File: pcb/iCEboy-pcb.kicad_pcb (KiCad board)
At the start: 2 copper layers, 51 x 61 mm, 64 parts, among them J1 dmg-card, J2 PROG_PORT, Q1 2N7002K, U1 TC74LCXR163245FT, U2 TC74LCXR163245FT, U3 ICE40UP5K-SG48ITR, U4 TPS79901DDCR, U5 TPS79901DDCR, U6 W25Q80DVSSIG, X1 SIT2001B

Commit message: modify value fields
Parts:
- C17: value C -> DNP
- J1: value dmg-card -> DMG_CARD
- R10, R11, R12, R13, R2: value 10k -> 10kΩ
- R3: value 2.2k -> 2.2kΩ
- R7: value 100Ω -> 1kΩ
- R8, R9: value R -> DNP

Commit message: modify decoup C value
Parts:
- C22, C26: value 2.2μF -> 4.7μF

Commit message: change value of X1
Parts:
- X1: value SIT2001B -> SIT2001B 20MHz

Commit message: update LED current limiting resistors
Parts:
- D1: value YELLOW -> SML-E12Y8WT86
- D2: value RED -> SML-E12V8WT86
- D3: value GREEN -> SML-E12P8WT86
- D4: value BLUE -> SMLE13BC8TT86
- R5: value 2.2kΩ -> 680Ω
- R6: value 2.2kΩ -> 4.7kΩ

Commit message: swap C11 C14 value
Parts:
- C11: value 10nF -> 1μF
- C14: value 1μF -> 10nF

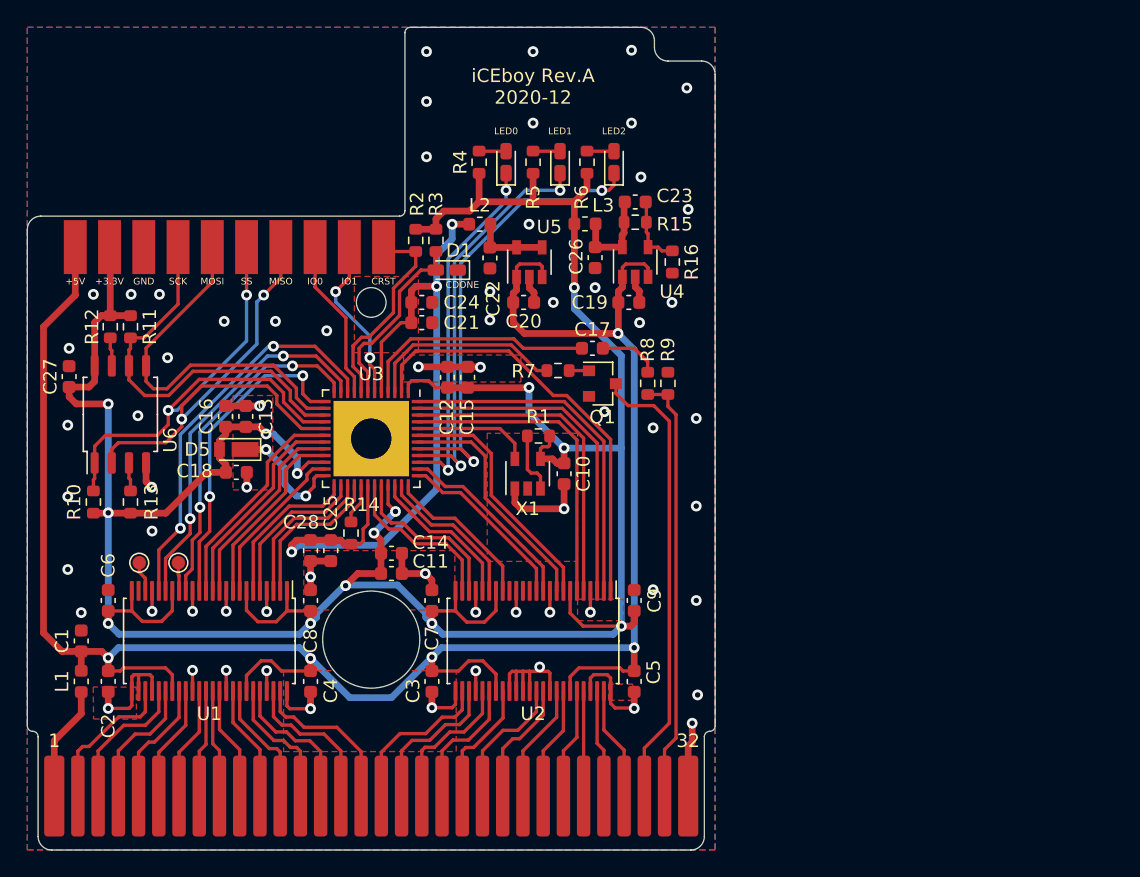
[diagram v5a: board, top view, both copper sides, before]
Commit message: migrate to KiCAD 6.0
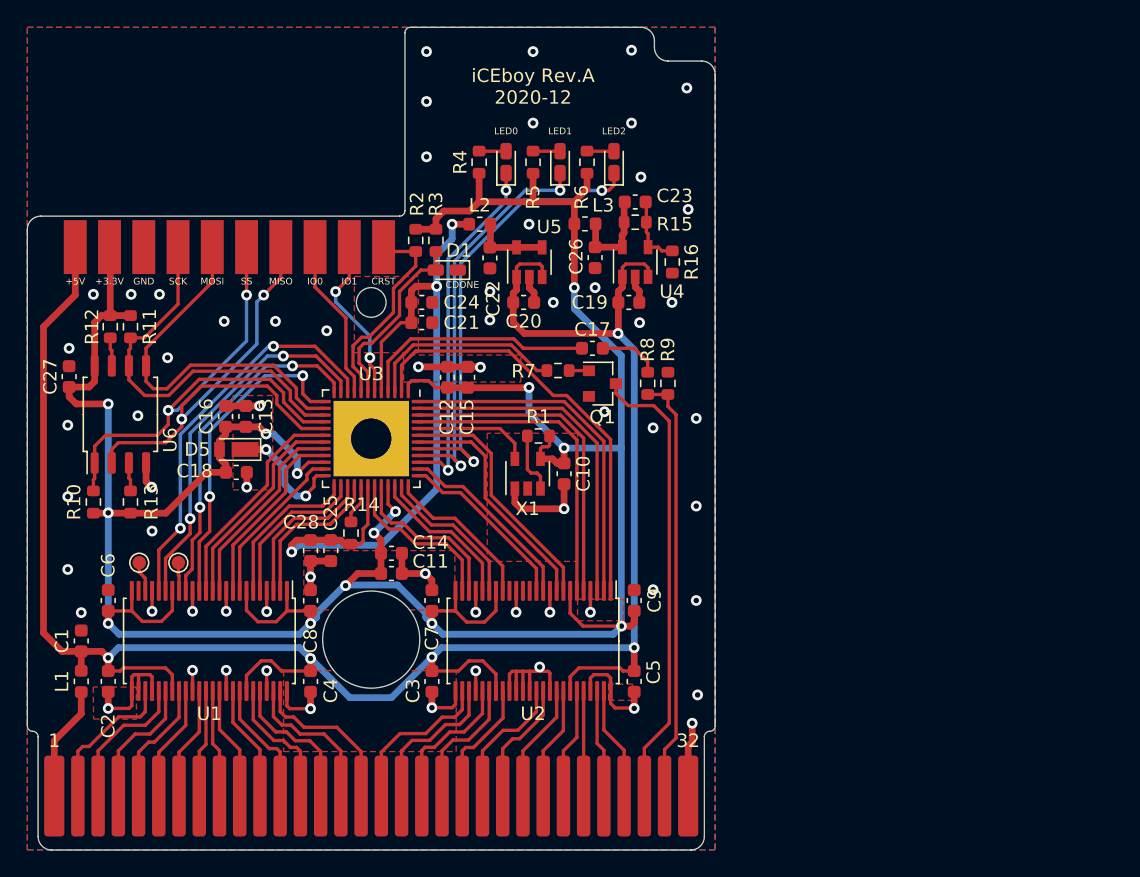
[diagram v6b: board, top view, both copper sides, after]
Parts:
- J1: value DMG_CARD -> DMG-CardEdge; footprint dmg-card:dmg-card -> DMG-CardEdge:DMG-CardEdge
- TP2: value ~CS -> ~{CS}
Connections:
- net /A0 renamed /CB-A0
- net /A0B renamed /DV-A0
- net /A1 renamed /CB-A1
- net /A10 renamed /CB-A10
- net /A10B renamed /DV-A10
- net /A11 renamed /CB-A11
- net /A11B renamed /DV-A11
- net /A12 renamed /CB-A12
- net /A12B renamed /DV-A12
- net /A13 renamed /CB-A13
- net /A13B renamed /DV-A13
- net /A14 renamed /CB-A14
- net /A14B renamed /DV-A14
- net /A15 renamed /CB-A15
- net /A15B renamed /DV-A15
- net /A1B renamed /DV-A1
- net /A2 renamed /CB-A2
- net /A2B renamed /DV-A2
- net /A3 renamed /CB-A3
- net /A3B renamed /DV-A3
- net /A4 renamed /CB-A4
- net /A4B renamed /DV-A4
- net /A5 renamed /CB-A5
- net /A5B renamed /DV-A5
- net /A6 renamed /CB-A6
- net /A6B renamed /DV-A6
- net /A7 renamed /CB-A7
- net /A7B renamed /DV-A7
- net /A8 renamed /CB-A8
- net /A8B renamed /DV-A8
- net /A9 renamed /CB-A9
- net /A9B renamed /DV-A9
- net /CLK renamed /CB-CLK
- net /CLKB renamed /DV-CLK
- net /D0 renamed /CB-D0
- net /D0B renamed /DV-D0
- net /D1 renamed /CB-D1
- net /D1B renamed /DV-D1
- net /D2 renamed /CB-D2
- net /D2B renamed /DV-D2
- net /D3 renamed /CB-D3
- net /D3B renamed /DV-D3
- net /D4 renamed /CB-D4
- net /D4B renamed /DV-D4
- net /D5 renamed /CB-D5
- net /D5B renamed /DV-D5
- net /D6 renamed /CB-D6
- net /D6B renamed /DV-D6
- net /D7 renamed /CB-D7
- net /D7B renamed /DV-D7
- net /EXT_CLK renamed /SYSCLK
- net /SPI_MISO renamed /SPI-MISO
- net /SPI_MOSI renamed /SPI-MOSI
- net /SPI_SCK renamed /SPI-SCK
- net /SPI_SS renamed /SPI-SS
- net /VIN renamed /CB-VIN
- net /VINB renamed /DV-VIN
- net /~CRESET renamed /~{CRESET}
- net /~CS renamed /CB-~{CS}
- net /~CS~B renamed /DV-~{CS}
- net /~RD renamed /CB-~{RD}
- net /~RD~B renamed /DV-~{RD}
- net /~RST renamed /CB-~{RST}
- net /~RST~B renamed /DV-~{RST}
- net /~WR renamed /CB-~{WR}
- net /~WR~B renamed /DV-~{WR}
- U1 pad 23: (no net) -> unconnected-(U1-Pad23)
- U2 pad 13: (no net) -> unconnected-(U2-Pad13)
- U2 pad 14: (no net) -> unconnected-(U2-Pad14)
- U2 pad 16: (no net) -> unconnected-(U2-Pad16)
- X1 pad 2: (no net) -> unconnected-(X1-Pad2)
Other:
- net class Bold removed
- net class Default removed

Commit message: update pcb wip
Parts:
- removed L1, L2, L3: 600Ω, Inductor_SMD:L_0603_1608Metric
- removed the R1 at (72.4, 64.8)
- removed the R9 at (82.0, 60.9)
- added C17: 1nF, Capacitor_SMD:C_0402_1005Metric, F.Cu at (113.2, 62.5)
- added C18: 1nF, Capacitor_SMD:C_0402_1005Metric, F.Cu at (113.2, 60.5)
- added FB1: MPZ1608S601ATA00, Inductor_SMD:L_0603_1608Metric, F.Cu at (38.9, 82.6)
- added FB2: MPZ1608S601ATA00, Inductor_SMD:L_0603_1608Metric, F.Cu at (68.0, 49.1)
- added FB3: MPZ1608S601ATA00, Inductor_SMD:L_0603_1608Metric, F.Cu at (75.8, 49.1)
- added R8: 8.2kΩ, Resistor_SMD:R_0402_1005Metric, F.Cu at (113.7, 58.0)
- C10, C12, C16, C2, C3, C4, C5, C6, C7, C8, C9: footprint Capacitor_SMD:C_0603_1608Metric -> Capacitor_SMD:C_0402_1005Metric
- C11: renamed from C15; footprint Capacitor_SMD:C_0603_1608Metric -> Capacitor_SMD:C_0402_1005Metric
- C13: renamed from C14; footprint Capacitor_SMD:C_0603_1608Metric -> Capacitor_SMD:C_0402_1005Metric
- C14: renamed from C13; footprint Capacitor_SMD:C_0603_1608Metric -> Capacitor_SMD:C_0402_1005Metric
- C15: renamed from C11; footprint Capacitor_SMD:C_0603_1608Metric -> Capacitor_SMD:C_0402_1005Metric
- C19: renamed from C17; value DNP -> 1uF; footprint Capacitor_SMD:C_0603_1608Metric -> Capacitor_SMD:C_0402_1005Metric
- C20: renamed from C18; footprint Capacitor_SMD:C_0603_1608Metric -> Capacitor_SMD:C_0402_1005Metric
- C21: renamed from C19; footprint Capacitor_SMD:C_0603_1608Metric -> Capacitor_SMD:C_0402_1005Metric
- C22: renamed from C20; footprint Capacitor_SMD:C_0603_1608Metric -> Capacitor_SMD:C_0402_1005Metric
- C23: renamed from C21; footprint Capacitor_SMD:C_0603_1608Metric -> Capacitor_SMD:C_0402_1005Metric
- C24: renamed from C22; footprint Capacitor_SMD:C_0603_1608Metric -> Capacitor_SMD:C_0402_1005Metric
- C25: renamed from C27; footprint Capacitor_SMD:C_0603_1608Metric -> Capacitor_SMD:C_0402_1005Metric
- C26: renamed from C24; footprint Capacitor_SMD:C_0603_1608Metric -> Capacitor_SMD:C_0402_1005Metric
- C27: renamed from C25; footprint Capacitor_SMD:C_0603_1608Metric -> Capacitor_SMD:C_0402_1005Metric
- C28: renamed from C23; footprint Capacitor_SMD:C_0603_1608Metric -> Capacitor_SMD:C_0402_1005Metric
- C30: renamed from C26; footprint Capacitor_SMD:C_0603_1608Metric -> Capacitor_SMD:C_0402_1005Metric
- R1: renamed from R2; footprint Resistor_SMD:R_0603_1608Metric -> Resistor_SMD:R_0402_1005Metric
- R10: renamed from R13; footprint Resistor_SMD:R_0603_1608Metric -> Resistor_SMD:R_0402_1005Metric
- R11, R12, R3: footprint Resistor_SMD:R_0603_1608Metric -> Resistor_SMD:R_0402_1005Metric
- R13: renamed from R14; footprint Resistor_SMD:R_0603_1608Metric -> Resistor_SMD:R_0402_1005Metric
- R14: renamed from R15; footprint Resistor_SMD:R_0603_1608Metric -> Resistor_SMD:R_0402_1005Metric
- R15: renamed from R16; footprint Resistor_SMD:R_0603_1608Metric -> Resistor_SMD:R_0402_1005Metric
- R2: renamed from R8; value DNP -> 8.2kΩ; footprint Resistor_SMD:R_0603_1608Metric -> Resistor_SMD:R_0402_1005Metric
- R4: renamed from R7; footprint Resistor_SMD:R_0603_1608Metric -> Resistor_SMD:R_0402_1005Metric
- R5: renamed from R4; footprint Resistor_SMD:R_0603_1608Metric -> Resistor_SMD:R_0402_1005Metric
- R6: renamed from R5; footprint Resistor_SMD:R_0603_1608Metric -> Resistor_SMD:R_0402_1005Metric
- R7: renamed from R6; footprint Resistor_SMD:R_0603_1608Metric -> Resistor_SMD:R_0402_1005Metric
- R9: renamed from R10; footprint Resistor_SMD:R_0603_1608Metric -> Resistor_SMD:R_0402_1005Metric
- X1: value SIT2001B 20MHz -> SG-210STF 20MHz; footprint Package_TO_SOT_SMD:SOT-23-5 -> Oscillator:Oscillator_SMD_SeikoEpson_SG210-4Pin_2.5x2.0mm
- moved J2 11.4 mm to (38.1, 50.4)
- moved C20 5.59 mm to (53.9, 71.5), turned to 45 degrees
- moved D5 5.33 mm to (53.4, 69.9), turned to -135 degrees
- moved C16 4.72 mm to (51.7, 67.3), turned to -90 degrees
- moved C14 4.47 mm to (52.7, 67.3), turned to -90 degrees
- moved C29 3.15 mm to (58.6, 73.4), turned to 180 degrees
- moved C15 3.15 mm to (62.3, 72.0)
- moved C25 2.76 mm to (39.1, 62.7), turned to -90 degrees
- moved C13 2.74 mm to (62.3, 70.9)
- moved C27 2.45 mm to (59.1, 72.0), turned to 180 degrees
- moved C10 1.76 mm to (73.0, 66.4), turned to 90 degrees
- moved R9 1.74 mm to (40.7, 68.6)
- moved C11 1.67 mm to (65.5, 60.2)
- moved R10 1.58 mm to (43.3, 68.6)
- moved R12 1.36 mm to (42.0, 56.9)
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- renumbered C28 to C29, D2 to D1, D3 to D2, D4 to D3, D1 to D4
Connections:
- C19 pad 1: Net-(C17-Pad1) -> /CB-VIN
- C19 pad 2: /DV-VIN -> Net-(C18-Pad1)
- R2 pad 1: /CB-VIN -> Net-(C17-Pad1)
- R2 pad 2: Net-(C17-Pad1) -> /DV-VIN
- X1 pad 1: GND -> unconnected-(X1-Pad1)
- X1 pad 2: unconnected-(X1-Pad2) -> GND
- X1 pad 3: Net-(R1-Pad1) -> /SYSCLK
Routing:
- net +3V3: track 225.2 -> 176.5 mm, vias 14 -> 9
- net Net-(C17-Pad1): track 4.51 -> 31.9 mm
- net /CB-VIN: track 31.9 -> 4.51 mm
- net GND: track 88.8 -> 71.0 mm, vias 64 -> 61
- net Net-(C18-Pad1): track 0.00 -> 17.6 mm
- net /DV-VIN: track 17.6 -> 0.00 mm
- net +1V2: track 55.5 -> 46.5 mm
- net /VPP: track 9.08 -> 3.40 mm, vias 2 -> 0
- net /SPI-MISO: track 37.1 -> 32.4 mm
- net /SPI-SS: track 39.7 -> 35.0 mm
- net Net-(R1-Pad1): track 4.57 -> 0.00 mm
- net /SPI-MOSI: track 27.9 -> 24.4 mm, vias 0 -> 2
- net /SPI-SCK: track 29.5 -> 26.1 mm, vias 0 -> 2
- net /DV-A5: track 13.9 -> 16.6 mm
- net /DV-A4: track 14.9 -> 17.6 mm
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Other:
- board text added: "------ Rev.B 2022-05"
- board text added: "TODO relocation / rewiring for 1005 components add board information silk fix U3 GND pad adjust reference font size"
- board text removed: "iCEboy Rev.A 2020-12"

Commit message: update pcb wip
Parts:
- D5: value RSX101VAM-30TR -> BAT43XV2; footprint Diode_SMD:D_TUMD2 -> Diode_SMD:D_SOD-523
- U3: footprint Package_DFN_QFN:QFN-48-1EP_7x7mm_P0.5mm_EP5.6x5.6mm -> Package_DFN_QFN:QFN-48-1EP_7x7mm_P0.5mm_EP5.6x5.6mm_ThermalVias
- moved C17 45.2 mm to (68.4, 57.1), turned to 180 degrees
- moved R8 43.2 mm to (70.5, 58.3), turned to 180 degrees
- moved C18 42.9 mm to (70.5, 57.1), turned to 180 degrees
- moved R2 12.4 mm to (68.4, 58.3), turned to 180 degrees
- moved Q1 11.1 mm to (79.5, 71.8)
- moved R5 10.0 mm to (78.0, 45.1)
- moved D1 10.0 mm to (80.0, 44.5)
- moved R4 9.55 mm to (77.9, 68.6), turned to -90 degrees
- moved D4 8.35 mm to (68.0, 44.5), turned to 90 degrees
- moved R7 6.04 mm to (70.0, 45.1)
- moved D3 6.00 mm to (72.0, 44.5)
- moved R3 5.29 mm to (66.0, 45.1), turned to 90 degrees
- moved C19 4.33 mm to (72.1, 58.8), turned to 90 degrees
- moved C10 3.68 mm to (69.7, 68.1), turned to 0 degrees
- moved R1 3.13 mm to (66.0, 48.7)
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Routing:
- net /CB-VIN: track 4.51 -> 35.7 mm
- net Net-(C17-Pad1): track 31.9 -> 2.24 mm
- net +3V3: track 176.5 -> 203.7 mm, vias 9 -> 11
- net Net-(C18-Pad1): track 17.6 -> 2.25 mm
- net /CDONE: track 13.9 -> 27.6 mm, vias 0 -> 2
- net /CB-~{RST}: track 33.6 -> 20.0 mm
- net /~{CRESET}: track 14.8 -> 23.7 mm, vias 0 -> 2
- net /RGB0: track 26.3 -> 35.0 mm
- net /DV-VIN: track 0.00 -> 8.65 mm
- net /RGB2: track 34.3 -> 26.3 mm
- net /DV-~{RST}: track 14.8 -> 21.9 mm
- net /DIR: track 31.8 -> 28.7 mm
- net /SYSCLK: track 8.13 -> 5.98 mm
- net +1V2: track 46.5 -> 48.2 mm, vias 3 -> 2
- net GND: track 71.0 -> 72.6 mm, vias 61 -> 52
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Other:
- board text added: "3.3V"
- board text added: "5V"
- board text added: "PCB thickness: 0.8mm"
- board text added: "Rev.B 2022-05"
- board text added: "TODO relocation / rewiring for 1005 components add board information silk"
- board text added: "USER LED"
- board text added: "icicleGB"
- board text removed: "+3.3V"
- board text removed: "+5V"
- board text removed: "------ Rev.B 2022-05"
- board text removed: "LED0"
- board text removed: "LED1"
- board text removed: "LED2"
- board text removed: "TODO relocation / rewiring for 1005 components add board information silk fix U3 GND pad adjust reference font size"
